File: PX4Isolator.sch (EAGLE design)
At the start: 22 parts, among them J1 DF13C-6P-1.25V, J2 DF13-4P-1.25V, J201 DF13C-6P-1.25V, J403 DF13C-7P-1.25V

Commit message: Isolator peripheral side signals done
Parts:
- removed C1001, C1003, C1004: 1u0, pixhawk2:CAP0603
- removed C1002: 10n, pixhawk2:CAP0402
- removed J201: DF13C-6P-1.25V, con-hirose-df13:DF13-6P-1.25V
- removed J403: DF13C-7P-1.25V, con-hirose-df13:DF13-7P-1.25V
- removed L2: NUF8402MN, PX4lite:NUF8402MN
- removed L201: KNH16C104DA5TS, pixhawk2:KNH16C104DA5TS
- removed U$1002: MIC5332, pixhawk2:MIC5332
- removed U$201: PESD0402-140, pixhawk2:DIODE-TVS
- added C10, C8, C9: 1u0, pixhawk2:CAP0603
- added C4, C5, C6: 0u1, pixhawk2:CAP0402
- added C7: 10n, pixhawk2:CAP0402
- added J3, J6: DF13C-7P-1.25V, con-hirose-df13:DF13-7P-1.25V
- added J4: DF13-4P-1.25V, con-hirose-df13:DF13-4P-1.25V
- added J5: DF13C-6P-1.25V, con-hirose-df13:DF13-6P-1.25V
- added R3, R4: 1K5, pixhawk2:RESISTOR0402-RES
- added U$2: MIC5332, pixhawk2:MIC5332
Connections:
- removed net !SPI_EXT_NSS: J403.5
- removed net FMU-I2C_SCL: J2.2, R1.1
- removed net FMU-I2C_SDA: J2.3, R2.1
- removed net FMU-USART2_CTS: L2G$8.P$1
- removed net FMU-USART2_RTS: L2G$7.P$1
- removed net FMU-USART2_RX: L2G$5.P$1
- removed net FMU-USART2_TX: L2G$6.P$1
- removed net FMU-USART3_CTS: L2G$2.P$1
- removed net FMU-USART3_RTS: L2G$1.P$1
- removed net FMU-USART3_RX: L2G$3.P$1
- removed net FMU-USART3_TX: L2G$4.P$1
- removed net FMU-VDD_5V: C1001.1, U$1002.EN1, U$1002.EN2, U$1002.VIN
- removed net GNDX: C1.2, C1001.2, C1002.2, C1003.2, C1004.2, C3.2, GND..P$1, J1.6, J201.6, J403.7, L201.P$3, U$1002.GND, U$201.A
- removed net GPIO_EXT_1: J403.6
- removed net N$104: C1002.1, U$1002.CSET
- removed net N$5: J201.1, L201.P$2, U$201.C
- removed net SERIAL1_CTS: J201.4, L2G$8.P$2
- removed net SERIAL1_RTS: J201.5, L2G$7.P$2
- removed net SERIAL1_RX: J201.3, L2G$5.P$2
- removed net SERIAL1_TX: J201.2, L2G$6.P$2
- removed net SERIAL2_CTS: J1.4, L2G$2.P$2
- removed net SERIAL2_RTS: J1.5, L2G$1.P$2
- removed net SERIAL2_RX: J1.3, L2G$3.P$2
- removed net SERIAL2_TX: J1.2, L2G$4.P$2
- removed net SPI_EXT_MISO: J403.3
- removed net SPI_EXT_MOSI: J403.4
- removed net SPI_EXT_SCK: J403.2
- removed net VDD_3V3_PERIPH: C1004.1, U$1002.VOUT2
- removed net VDD_5V_HIPOWER: L201.P$1
- removed net VDD_5V_PERIPH: C1.1, C2.1, C3.1, J1.1, J2.1, J403.1
- new net GND_ISOL: C4.2, C5.2, C6.2, J4.4, J5.6, J6.7, U$1G$2.GNDB
- new net MASTER_IN1: J1.3, J3.3, U$1G$1.INA1
- new net MASTER_IN2: U$1G$1.INA2
- new net MASTER_IO1: J1.4, J2.2, J3.5, R1.1, U$1G$1.IOA1
- new net MASTER_IO2: J1.5, J2.3, J3.6, R2.1, U$1G$1.IOA2
- new net MASTER_OUT1: J1.2, J3.4, U$1G$1.OUTA1
- new net MASTER_OUT2: J3.2, U$1G$1.OUTA2
- new net N$1: C7.1, U$2.CSET
- new net PERIPH_IN1: J5.3, J6.3, U$1G$2.INB1
- new net PERIPH_IN2: U$1G$2.INB2
- new net PERIPH_IO1: J4.2, J5.4, J6.5, R3.1, U$1G$2.IOB1
- new net PERIPH_IO2: J4.3, J5.5, J6.6, R4.1, U$1G$2.IOB2
- new net PERIPH_OUT1: J5.2, J6.4, U$1G$2.OUTB1
- new net PERIPH_OUT2: J6.2, U$1G$2.OUTB2
- new net VDD_3V3_ISOL: U$1G$2.VCCB
- new net VDD_3V3_MASTER: C10.1, U$2.VOUT2
- new net VDD_5V_MASTER: C1.1, C2.1, C3.1, C4.1, C5.1, C6.1, C8.1, J1.1, J2.1, J3.1, J4.1, J5.1, J6.1, U$2.EN1, U$2.EN2, U$2.VIN
- net GND: now also C1.2, C10.2, C3.2, C7.2, C8.2, C9.2, GND..P$1, J1.6, J3.7, U$1G$1.GNDA, U$2.GND; no longer L2G$9.GND
- net VDD_3V3: now also C9.1, R3.2, R4.2, U$1G$1.VCCA, U$2.VOUT1; no longer C1003.1, U$1002.VOUT1
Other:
- note added: "!CS"
- note added: "!INT"
- note added: "CLK"
- note added: "CTS"
- note added: "MASTER CONNECTIONS"
- note added: "MISO"
- note added: "MOSI"
- note added: "RTS"
- note added: "RX"
- note added: "SCL"
- note added: "SDA"
- note added: "TX"
- note removed: "FMU_CONNECTIONS"
- note removed: "Note: SPI port is UNBUFFERED; only suitable for short connections."
- note removed: "SERIAL1"

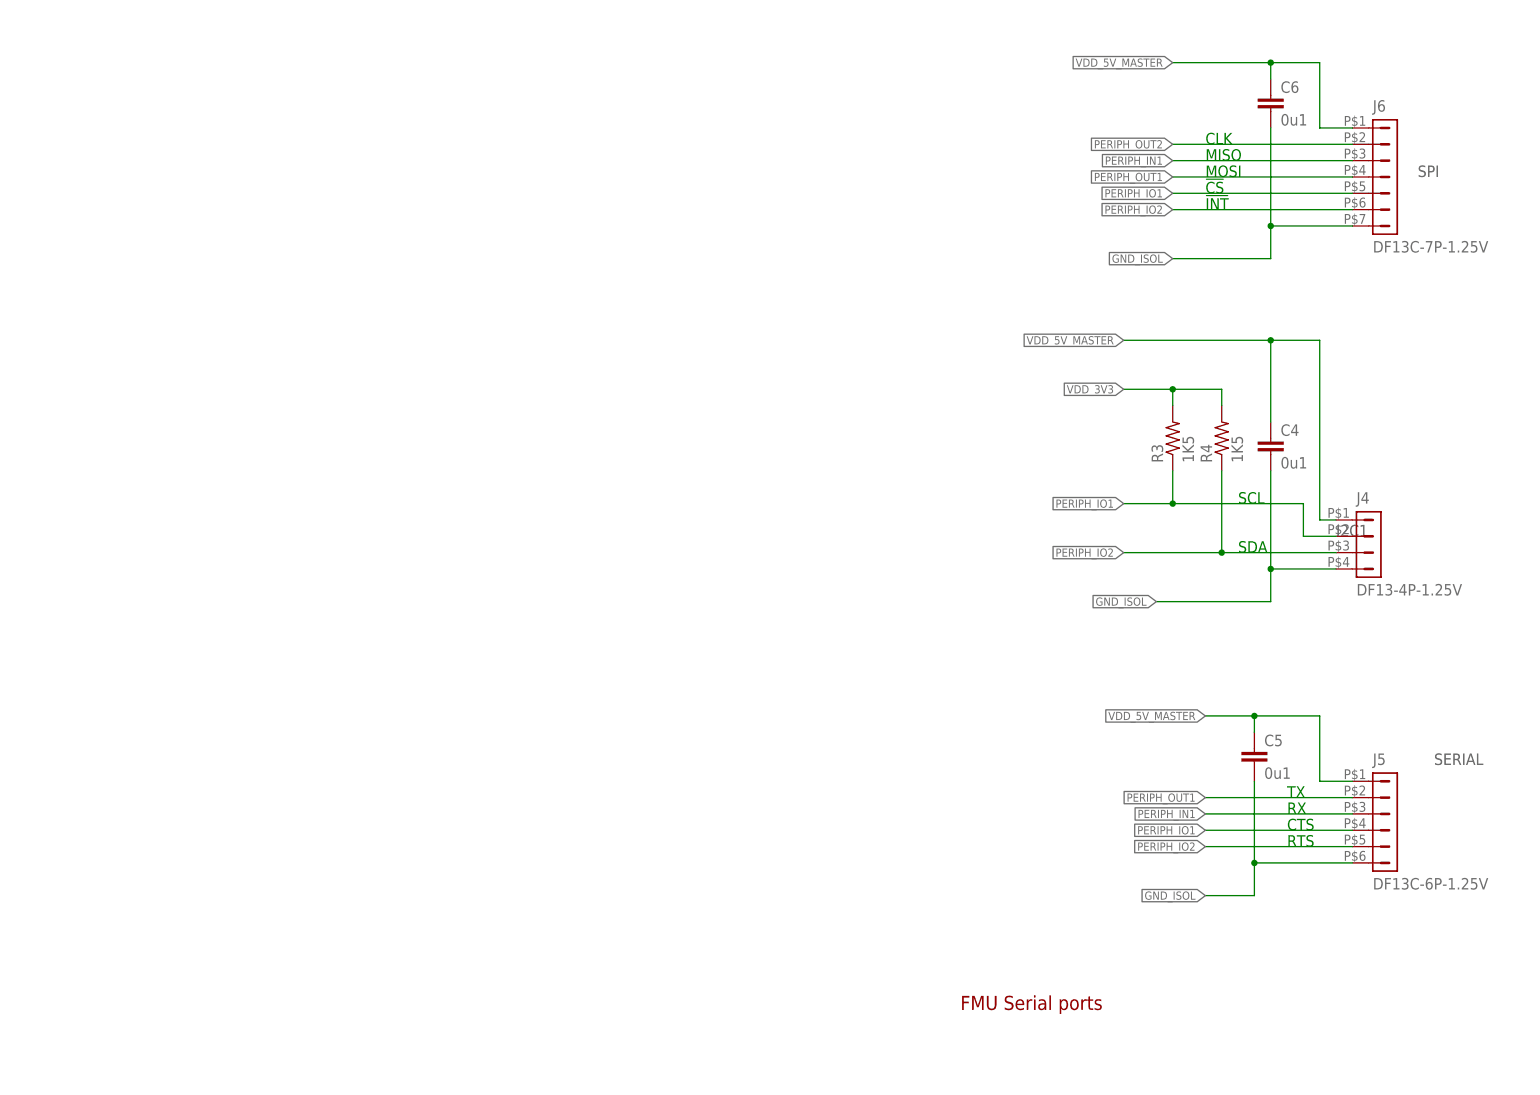
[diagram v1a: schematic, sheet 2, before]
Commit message: Regulator added
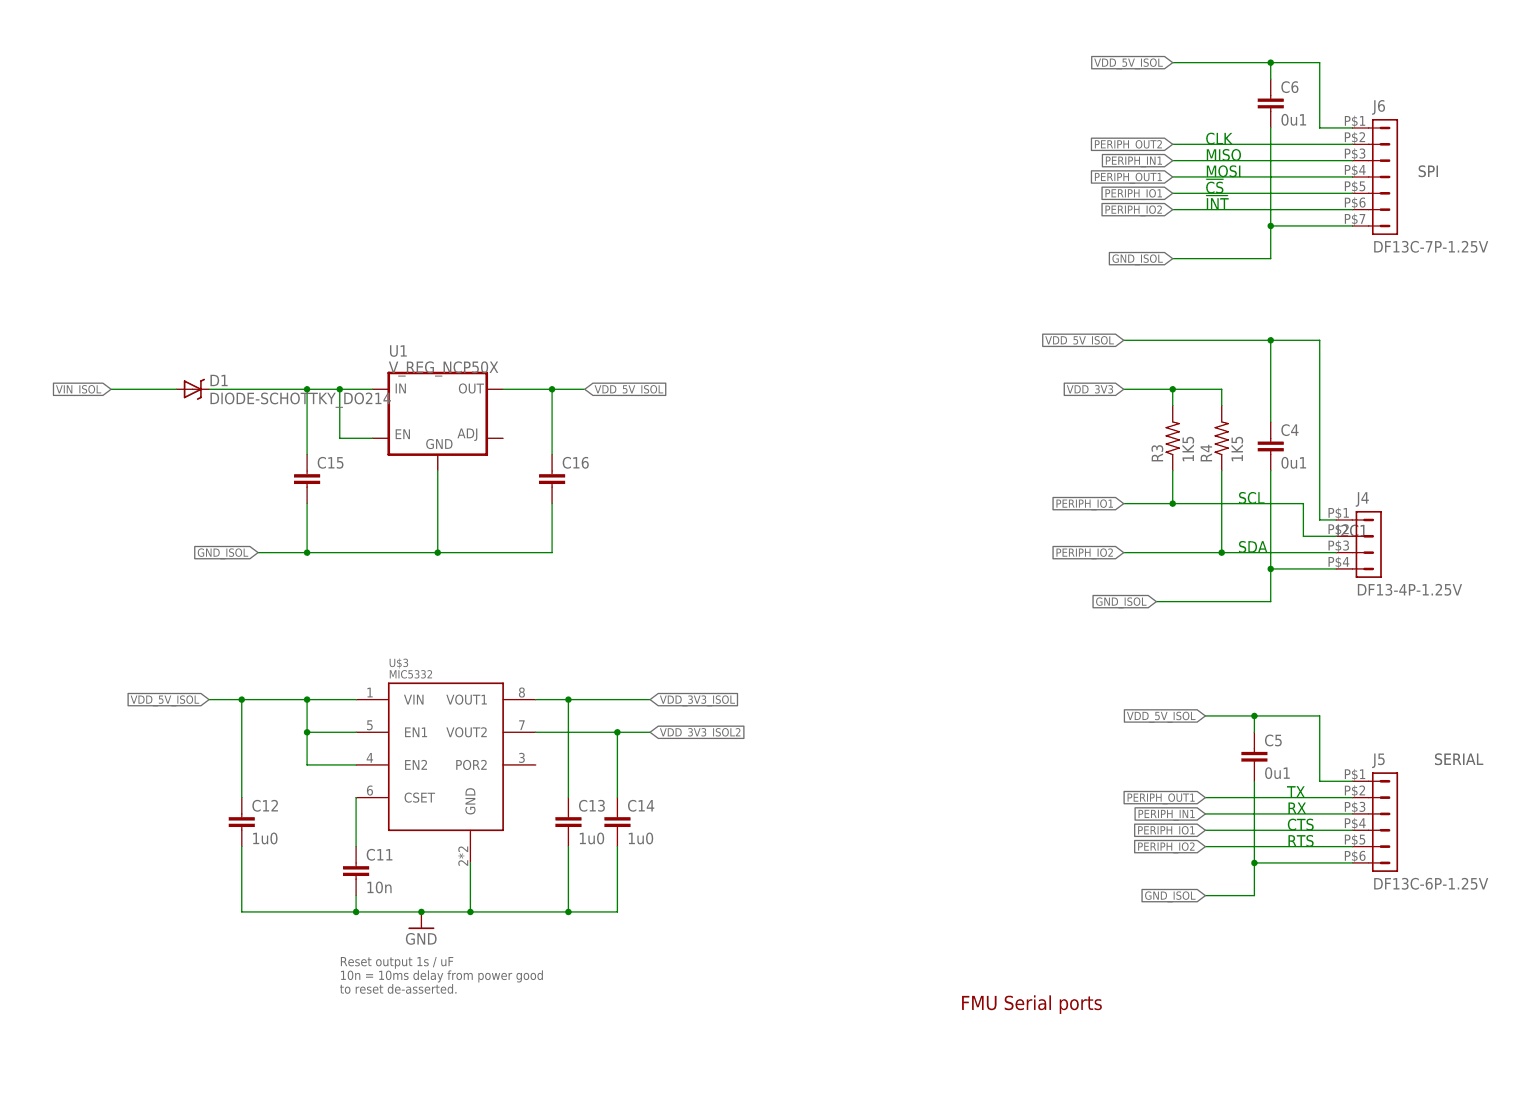
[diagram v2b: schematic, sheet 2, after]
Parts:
- added C11: 10n, pixhawk2:CAP0402
- added C12, C13, C14: 1u0, pixhawk2:CAP0603
- added C15, C16: (no value), PX4FMUlite_V0_1:CAP0603
- added D1: DIODE-SCHOTTKY_DO214, PX4FMUlite_V0_1:DIODE-SCHOTTKY_DO214
- added U$3: MIC5332, pixhawk2:MIC5332
- added U1: V_REG_NCP50X, SparkFun-PowerIC:V_REG_NCP50X
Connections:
- new net N$2: C11.1, U$3.CSET
- new net N$3: C15.1, D1.C, U1.EN, U1.IN
- new net VDD_3V3_ISOL2: C14.1, U$3.VOUT2
- new net VDD_5V_ISOL: C12.1, C16.1, C4.1, C5.1, C6.1, J4.1, J5.1, J6.1, U$3.EN1, U$3.EN2, U$3.VIN, U1.OUT
- new net VIN_ISOL: D1.A
- net GND: now also C11.2, C12.2, C13.2, C14.2, U$3.GND
- net GND_ISOL: now also C15.2, C16.2, U1.GND
- net VDD_3V3_ISOL: now also C13.1, U$3.VOUT1
- net VDD_5V_MASTER: no longer C4.1, C5.1, C6.1, J4.1, J5.1, J6.1
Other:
- moved on the sheet: C10, C9

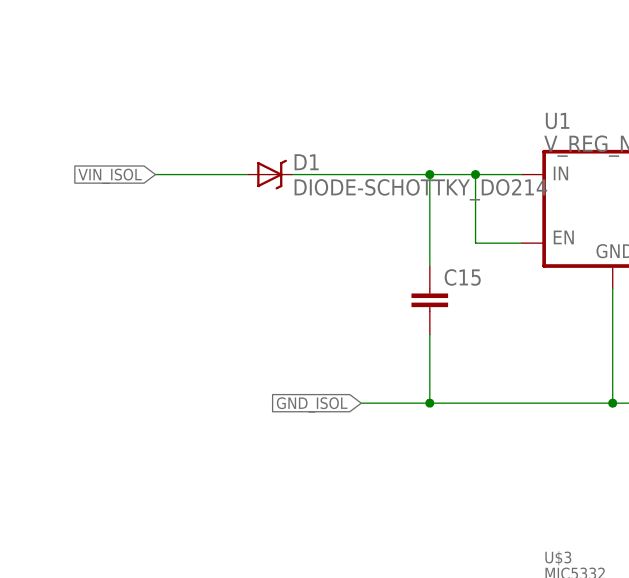
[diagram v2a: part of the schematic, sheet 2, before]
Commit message: Added TPS62143 buck, moved mounting points
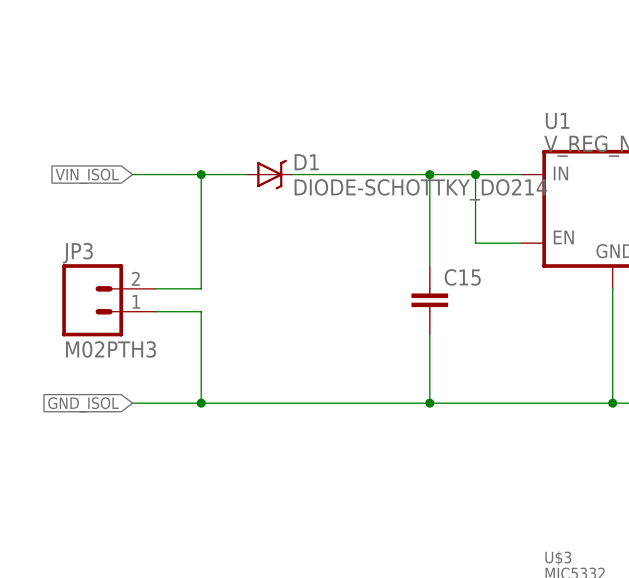
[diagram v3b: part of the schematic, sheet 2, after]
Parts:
- added JP3: M02PTH3, SparkFun-Connectors:M02PTH3
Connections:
- net GND_ISOL: now also JP3.1
- net VIN_ISOL: now also JP3.2
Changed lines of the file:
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@@
 <part name="C15" library="PX4FMUlite_V0_1" deviceset="CAP" device="0603"/>
 <part name="C16" library="PX4FMUlite_V0_1" deviceset="CAP" device="0603"/>
+<part name="JP3" library="SparkFun-Connectors" deviceset="M02" device="PTH3"/>
 </parts>
 <sheets>
@@
 <instance part="C15" gate="G$1" x="63.5" y="99.06"/>
 <instance part="C16" gate="G$1" x="101.6" y="99.06"/>
+<instance part="JP3" gate="G$1" x="25.4" y="99.06"/>
 </instances>
 <busses>
@@
 <segment>
 <wire x1="83.82" y1="88.9" x2="63.5" y2="88.9" width="0.1524" layer="91"/>
-<label x="55.88" y="88.9" size="1.27" layer="95" rot="R180" xref="yes"/>
+<label x="30.48" y="88.9" size="1.27" layer="95" rot="R180" xref="yes"/>
 <pinref part="U1" gate="G$1" pin="GND"/>
-<wire x1="63.5" y1="88.9" x2="55.88" y2="88.9" width="0.1524" layer="91"/>
+<wire x1="63.5" y1="88.9" x2="38.1" y2="88.9" width="0.1524" layer="91"/>
+<wire x1="38.1" y1="88.9" x2="30.48" y2="88.9" width="0.1524" layer="91"/>
 <wire x1="83.82" y1="101.6" x2="83.82" y2="88.9" width="0.1524" layer="91"/>
 <pinref part="C15" gate="G$1" pin="2"/>
@@
 <junction x="83.82" y="88.9"/>
 <junction x="63.5" y="88.9"/>
+<pinref part="JP3" gate="G$1" pin="1"/>
+<wire x1="33.02" y1="99.06" x2="38.1" y2="99.06" width="0.1524" layer="91"/>
+<wire x1="38.1" y1="99.06" x2="38.1" y2="88.9" width="0.1524" layer="91"/>
+<junction x="38.1" y="88.9"/>
 </segment>
 </net>
 <net name="VIN_ISOL" class="1">
 <segment>
-<wire x1="43.18" y1="114.3" x2="33.02" y2="114.3" width="0.1524" layer="91"/>
-<label x="33.02" y="114.3" size="1.27" layer="95" rot="R180" xref="yes"/>
+<wire x1="43.18" y1="114.3" x2="38.1" y2="114.3" width="0.1524" layer="91"/>
+<label x="30.48" y="114.3" size="1.27" layer="95" rot="R180" xref="yes"/>
 <pinref part="D1" gate="G$1" pin="A"/>
-</segment>
-</net>
+<pinref part="JP3" gate="G$1" pin="2"/>
+<wire x1="38.1" y1="114.3" x2="30.48" y2="114.3" width="0.1524" layer="91"/>
+<wire x1="33.02" y1="101.6" x2="38.1" y2="101.6" width="0.1524" layer="91"/>
+<wire x1="38.1" y1="101.6" x2="38.1" y2="114.3" width="0.1524" layer="91"/>
+<junction x="38.1" y="114.3"/>
+</segment>
+</net>
